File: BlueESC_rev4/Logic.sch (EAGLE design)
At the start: 37 parts, among them U1 ATMEGA168, U2 V_REG_LDOSMD, Y1 RESONATORSMD

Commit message: Commit before major changes to rev 4
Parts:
- R15: value 22 -> 150
- R16: value 22 -> 100
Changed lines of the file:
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@@
 <part name="GND9" library="SparkFun" deviceset="GND" device=""/>
 <part name="Y1" library="SparkFun" deviceset="RESONATOR" device="SMD"/>
-<part name="R15" library="SparkFun" deviceset="RESISTOR" device="0603-RES" value="22"/>
+<part name="R15" library="SparkFun" deviceset="RESISTOR" device="0603-RES" value="150"/>
 <part name="LED2" library="SparkFun" deviceset="LED" device="-3MM-NO_SILK" value="BLUE"/>
-<part name="R16" library="SparkFun" deviceset="RESISTOR" device="0603-RES" value="22"/>
+<part name="R16" library="SparkFun" deviceset="RESISTOR" device="0603-RES" value="100"/>
 <part name="LED1" library="SparkFun" deviceset="LED" device="-3MM-NO_SILK" value="RED"/>
 <part name="GND7" library="SparkFun" deviceset="GND" device=""/>

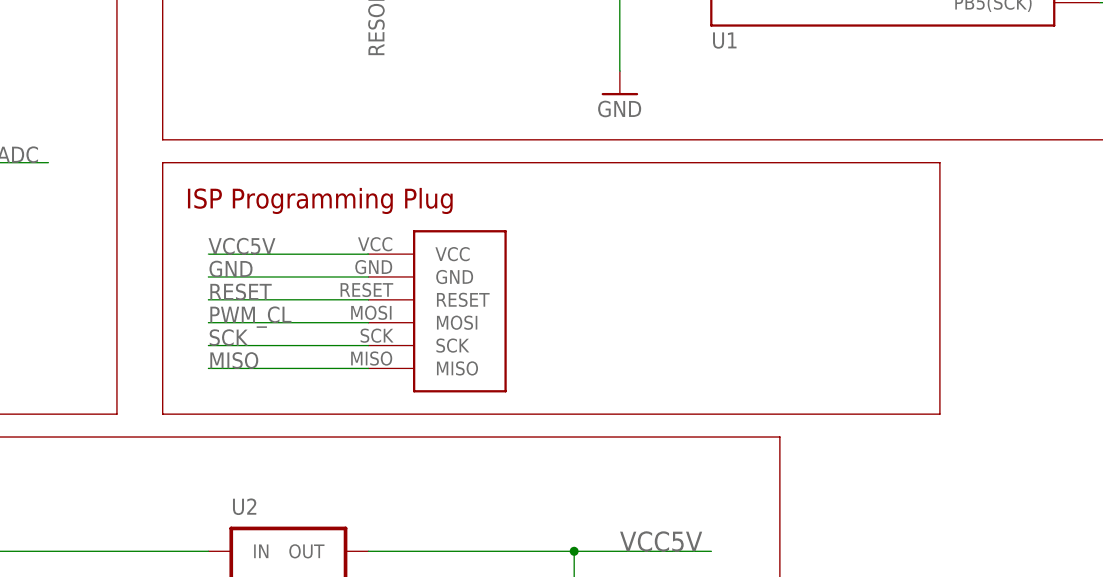
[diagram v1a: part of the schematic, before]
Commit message: Major updates on revision 4 include rearranged components, removal of programming pins, and new board shapes.
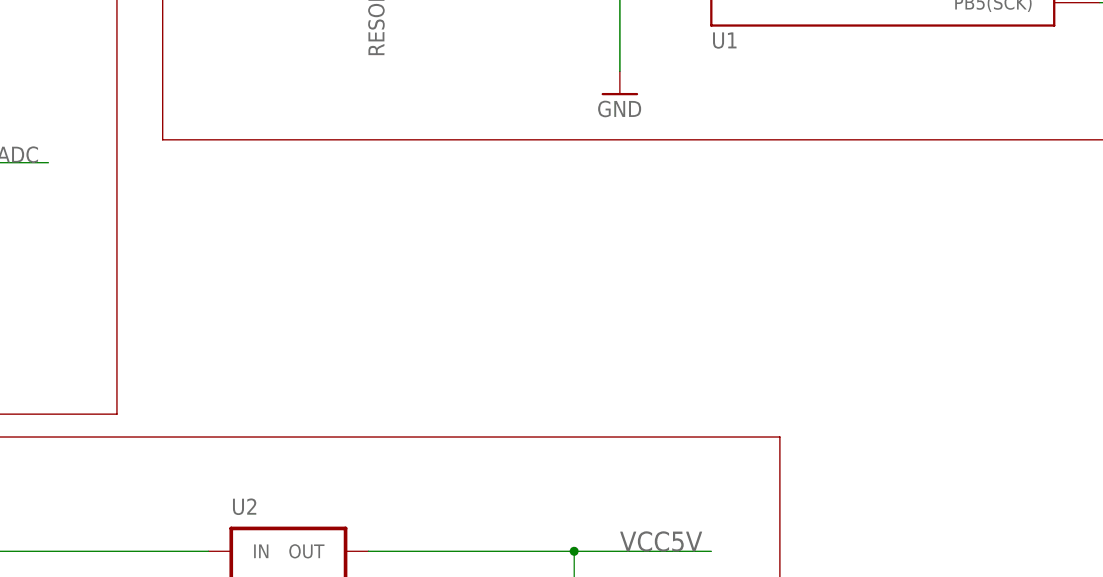
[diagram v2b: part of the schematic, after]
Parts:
- removed U$14: AVR-ISPTINY-SMD, BR-Eagle-Library:AVR-ISPTINY-SMD
- U$4: value LOGOBR-LOGO-S -> LOGOBR-LOGO-M; device BR-Eagle-Library:LOGOBR-LOGO-S -> BR-Eagle-Library:LOGOBR-LOGO-M
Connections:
- net GND: no longer U$14.GND
- net MISO: no longer U$14.MISO
- net PWM_CL: no longer U$14.MOSI
- net RESET: no longer U$14.RESET
- net SCK: no longer U$14.SCK
- net VCC5V: no longer U$14.VCC
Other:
- note removed: "ISP Programming Plug"
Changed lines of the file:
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@@
 <grid distance="0.1" unitdist="inch" unit="inch" style="lines" multiple="1" display="no" altdistance="0.01" altunitdist="inch" altunit="inch"/>
 <layers>
-<layer number="1" name="Top" color="4" fill="1" visible="no" active="no"/>
-<layer number="2" name="Route2" color="1" fill="3" visible="no" active="no"/>
-<layer number="3" name="Route3" color="4" fill="3" visible="no" active="no"/>
-<layer number="14" name="Route14" color="1" fill="6" visible="no" active="no"/>
-<layer number="15" name="Route15" color="4" fill="6" visible="no" active="no"/>
-<layer number="16" name="Bottom" color="1" fill="1" visible="no" active="no"/>
-<layer number="17" name="Pads" color="2" fill="1" visible="no" active="no"/>
-<layer number="18" name="Vias" color="2" fill="1" visible="no" active="no"/>
-<layer number="19" name="Unrouted" color="6" fill="1" visible="no" active="no"/>
-<layer number="20" name="Dimension" color="15" fill="1" visible="no" active="no"/>
-<layer number="21" name="tPlace" color="7" fill="1" visible="no" active="no"/>
-<layer number="22" name="bPlace" color="7" fill="1" visible="no" active="no"/>
-<layer number="23" name="tOrigins" color="15" fill="1" visible="no" active="no"/>
-<layer number="24" name="bOrigins" color="15" fill="1" visible="no" active="no"/>
-<layer number="25" name="tNames" color="7" fill="1" visible="no" active="no"/>
-<layer number="26" name="bNames" color="7" fill="1" visible="no" active="no"/>
-<layer number="27" name="tValues" color="7" fill="1" visible="no" active="no"/>
-<layer number="28" name="bValues" color="7" fill="1" visible="no" active="no"/>
+<layer number="1" name="Top" color="4" fill="1" visible="yes" active="no"/>
+<layer number="2" name="Route2" color="1" fill="3" visible="yes" active="no"/>
+<layer number="3" name="Route3" color="4" fill="3" visible="yes" active="no"/>
+<layer number="14" name="Route14" color="1" fill="6" visible="yes" active="no"/>
+<layer number="15" name="Route15" color="4" fill="6" visible="yes" active="no"/>
+<layer number="16" name="Bottom" color="1" fill="1" visible="yes" active="no"/>
+<layer number="17" name="Pads" color="2" fill="1" visible="yes" active="no"/>
+<layer number="18" name="Vias" color="2" fill="1" visible="yes" active="no"/>
+<layer number="19" name="Unrouted" color="6" fill="1" visible="yes" active="no"/>
+<layer number="20" name="Dimension" color="15" fill="1" visible="yes" active="no"/>
+<layer number="21" name="tPlace" color="7" fill="1" visible="yes" active="no"/>
+<layer number="22" name="bPlace" color="7" fill="1" visible="yes" active="no"/>
+<layer number="23" name="tOrigins" color="15" fill="1" visible="yes" active="no"/>
+<layer number="24" name="bOrigins" color="15" fill="1" visible="yes" active="no"/>
+<layer number="25" name="tNames" color="7" fill="1" visible="yes" active="no"/>
+<layer number="26" name="bNames" color="7" fill="1" visible="yes" active="no"/>
+<layer number="27" name="tValues" color="7" fill="1" visible="yes" active="no"/>
+<layer number="28" name="bValues" color="7" fill="1" visible="yes" active="no"/>
 <layer number="29" name="tStop" color="7" fill="3" visible="no" active="no"/>
 <layer number="30" name="bStop" color="7" fill="6" visible="no" active="no"/>
@@
 <layer number="35" name="tGlue" color="7" fill="4" visible="no" active="no"/>
 <layer number="36" name="bGlue" color="7" fill="5" visible="no" active="no"/>
-<layer number="37" name="tTest" color="7" fill="1" visible="no" active="no"/>
-<layer number="38" name="bTest" color="7" fill="1" visible="no" active="no"/>
+<layer number="37" name="tTest" color="7" fill="1" visible="yes" active="no"/>
+<layer number="38" name="bTest" color="7" fill="1" visible="yes" active="no"/>
 <layer number="39" name="tKeepout" color="4" fill="11" visible="no" active="no"/>
 <layer number="40" name="bKeepout" color="1" fill="11" visible="no" active="no"/>
@@
 <layer number="44" name="Drills" color="7" fill="1" visible="no" active="no"/>
 <layer number="45" name="Holes" color="7" fill="1" visible="no" active="no"/>
-<layer number="46" name="Milling" color="3" fill="1" visible="no" active="no"/>
-<layer number="47" name="Measures" color="7" fill="1" visible="no" active="no"/>
-<layer number="48" name="Document" color="7" fill="1" visible="no" active="no"/>
-<layer number="49" name="Reference" color="7" fill="1" visible="no" active="no"/>
-<layer number="50" name="dxf" color="7" fill="1" visible="no" active="no"/>
-<layer number="51" name="tDocu" color="7" fill="1" visible="no" active="no"/>
-<layer number="52" name="bDocu" color="7" fill="1" visible="no" active="no"/>
-<layer number="53" name="tGND_GNDA" color="7" fill="9" visible="no" active="no"/>
-<layer number="54" name="bGND_GNDA" color="1" fill="9" visible="no" active="no"/>
-<layer number="56" name="wert" color="7" fill="1" visible="no" active="no"/>
-<layer number="57" name="tCAD" color="7" fill="1" visible="no" active="no"/>
+<layer number="46" name="Milling" color="3" fill="1" visible="yes" active="no"/>
+<layer number="47" name="Measures" color="7" fill="1" visible="yes" active="no"/>
+<layer number="48" name="Document" color="7" fill="1" visible="yes" active="no"/>
+<layer number="49" name="Reference" color="7" fill="1" visible="yes" active="no"/>
+<layer number="50" name="dxf" color="7" fill="1" visible="yes" active="no"/>
+<layer number="51" name="tDocu" color="7" fill="1" visible="yes" active="no"/>
+<layer number="52" name="bDocu" color="7" fill="1" visible="yes" active="no"/>
+<layer number="53" name="tGND_GNDA" color="7" fill="9" visible="yes" active="no"/>
+<layer number="54" name="bGND_GNDA" color="1" fill="9" visible="yes" active="no"/>
+<layer number="56" name="wert" color="7" fill="1" visible="yes" active="no"/>
+<layer number="57" name="tCAD" color="7" fill="1" visible="yes" active="no"/>
 <layer number="91" name="Nets" color="2" fill="1" visible="yes" active="yes"/>
 <layer number="92" name="Busses" color="1" fill="1" visible="yes" active="yes"/>
@@
 <part name="GND21" library="SparkFun-Aesthetics" deviceset="GND" device=""/>
 <part name="GND22" library="SparkFun-Aesthetics" deviceset="GND" device=""/>
-<part name="U$4" library="BR-Eagle-Library" deviceset="LOGO" device="BR-LOGO-S" value="LOGOBR-LOGO-S"/>
+<part name="U$4" library="BR-Eagle-Library" deviceset="LOGO" device="BR-LOGO-M" value="LOGOBR-LOGO-M"/>
 <part name="U$3" library="BR-Eagle-Library" deviceset="PAD" device="1.5X3MM"/>
 <part name="U$8" library="BR-Eagle-Library" deviceset="PAD" device="1.5X3MM"/>
@@
 <part name="U$12" library="BR-Eagle-Library" deviceset="PAD" device="1.5X3MM"/>
 <part name="U$13" library="BR-Eagle-Library" deviceset="PAD" device="1.5X3MM"/>
-<part name="U$14" library="BR-Eagle-Library" deviceset="AVR-ISP" device="TINY-SMD"/>
 <part name="LOGO1" library="SparkFun-Aesthetics" deviceset="OSHW-LOGO" device="S"/>
 <part name="C4" library="SparkFun-Capacitors" deviceset="CAP" device="0603-CAP" value="0.1uF"/>
@@
 <wire x1="68.58" y1="198.12" x2="68.58" y2="261.62" width="0.1524" layer="94"/>
 <text x="71.12" y="256.54" size="2.1844" layer="94" ratio="13">Phase Sensing</text>
-<wire x1="40.64" y1="86.36" x2="127" y2="86.36" width="0.1524" layer="94"/>
-<wire x1="127" y1="86.36" x2="127" y2="58.42" width="0.1524" layer="94"/>
-<wire x1="127" y1="58.42" x2="40.64" y2="58.42" width="0.1524" layer="94"/>
-<wire x1="40.64" y1="58.42" x2="40.64" y2="86.36" width="0.1524" layer="94"/>
-<text x="43.18" y="81.28" size="2.1844" layer="94" ratio="13">ISP Programming Plug</text>
 <wire x1="-10.16" y1="124.46" x2="35.56" y2="124.46" width="0.1524" layer="94"/>
 <wire x1="35.56" y1="124.46" x2="35.56" y2="58.42" width="0.1524" layer="94"/>
@@
 <instance part="U$12" gate="G$1" x="43.18" y="-2.54"/>
 <instance part="U$13" gate="G$1" x="43.18" y="-10.16"/>
-<instance part="U$14" gate="G$1" x="68.58" y="60.96"/>
 <instance part="LOGO1" gate="G$1" x="88.9" y="-25.4"/>
 <instance part="C4" gate="G$1" x="190.5" y="63.5"/>
@@
 <wire x1="-5.08" y1="-2.54" x2="5.08" y2="-2.54" width="0.1524" layer="91"/>
 <label x="-5.08" y="-2.54" size="1.778" layer="95"/>
-</segment>
-<segment>
-<pinref part="U$14" gate="G$1" pin="GND"/>
-<wire x1="45.72" y1="73.66" x2="63.5" y2="73.66" width="0.1524" layer="91"/>
-<label x="45.72" y="73.66" size="1.778" layer="95"/>
 </segment>
 <segment>
@@
 </segment>
 <segment>
-<pinref part="U$14" gate="G$1" pin="VCC"/>
-<wire x1="63.5" y1="76.2" x2="45.72" y2="76.2" width="0.1524" layer="91"/>
-<label x="45.72" y="76.2" size="1.778" layer="95"/>
-</segment>
-<segment>
 <pinref part="C4" gate="G$1" pin="1"/>
 <wire x1="190.5" y1="68.58" x2="190.5" y2="76.2" width="0.1524" layer="91"/>
@@
 <label x="50.8" y="-88.9" size="1.778" layer="95"/>
 <pinref part="U$17" gate="G$1" pin="10"/>
-</segment>
-<segment>
-<pinref part="U$14" gate="G$1" pin="MOSI"/>
-<wire x1="45.72" y1="68.58" x2="63.5" y2="68.58" width="0.1524" layer="91"/>
-<label x="45.72" y="68.58" size="1.778" layer="95"/>
 </segment>
 <segment>
@@
 <label x="154.94" y="106.68" size="1.778" layer="95"/>
 </segment>
-<segment>
-<pinref part="U$14" gate="G$1" pin="MISO"/>
-<wire x1="45.72" y1="63.5" x2="63.5" y2="63.5" width="0.1524" layer="91"/>
-<label x="45.72" y="63.5" size="1.778" layer="95"/>
-</segment>
 </net>
 <net name="SCK" class="0">
@@
 <wire x1="144.78" y1="104.14" x2="167.64" y2="104.14" width="0.1524" layer="91"/>
 <label x="154.94" y="104.14" size="1.778" layer="95"/>
-</segment>
-<segment>
-<pinref part="U$14" gate="G$1" pin="SCK"/>
-<wire x1="63.5" y1="66.04" x2="45.72" y2="66.04" width="0.1524" layer="91"/>
-<label x="45.72" y="66.04" size="1.778" layer="95"/>
 </segment>
 </net>
@@
 <label x="58.42" y="162.56" size="1.778" layer="95" ratio="9"/>
 </segment>
-<segment>
-<pinref part="U$14" gate="G$1" pin="RESET"/>
-<wire x1="45.72" y1="71.12" x2="63.5" y2="71.12" width="0.1524" layer="91"/>
-<label x="45.72" y="71.12" size="1.778" layer="95"/>
-</segment>
-</net>
+</net>

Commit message: Minor changes before ordering production boards.
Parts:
- R15: value 150 -> 2.2K
- R16: value 100 -> 150
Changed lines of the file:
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@@
 <grid distance="0.1" unitdist="inch" unit="inch" style="lines" multiple="1" display="no" altdistance="0.01" altunitdist="inch" altunit="inch"/>
 <layers>
-<layer number="1" name="Top" color="4" fill="1" visible="yes" active="no"/>
-<layer number="2" name="Route2" color="1" fill="3" visible="yes" active="no"/>
-<layer number="3" name="Route3" color="4" fill="3" visible="yes" active="no"/>
-<layer number="14" name="Route14" color="1" fill="6" visible="yes" active="no"/>
-<layer number="15" name="Route15" color="4" fill="6" visible="yes" active="no"/>
-<layer number="16" name="Bottom" color="1" fill="1" visible="yes" active="no"/>
-<layer number="17" name="Pads" color="2" fill="1" visible="yes" active="no"/>
-<layer number="18" name="Vias" color="2" fill="1" visible="yes" active="no"/>
-<layer number="19" name="Unrouted" color="6" fill="1" visible="yes" active="no"/>
-<layer number="20" name="Dimension" color="15" fill="1" visible="yes" active="no"/>
-<layer number="21" name="tPlace" color="7" fill="1" visible="yes" active="no"/>
-<layer number="22" name="bPlace" color="7" fill="1" visible="yes" active="no"/>
-<layer number="23" name="tOrigins" color="15" fill="1" visible="yes" active="no"/>
-<layer number="24" name="bOrigins" color="15" fill="1" visible="yes" active="no"/>
-<layer number="25" name="tNames" color="7" fill="1" visible="yes" active="no"/>
-<layer number="26" name="bNames" color="7" fill="1" visible="yes" active="no"/>
-<layer number="27" name="tValues" color="7" fill="1" visible="yes" active="no"/>
-<layer number="28" name="bValues" color="7" fill="1" visible="yes" active="no"/>
+<layer number="1" name="Top" color="4" fill="1" visible="no" active="no"/>
+<layer number="2" name="Route2" color="1" fill="3" visible="no" active="no"/>
+<layer number="3" name="Route3" color="4" fill="3" visible="no" active="no"/>
+<layer number="14" name="Route14" color="1" fill="6" visible="no" active="no"/>
+<layer number="15" name="Route15" color="4" fill="6" visible="no" active="no"/>
+<layer number="16" name="Bottom" color="1" fill="1" visible="no" active="no"/>
+<layer number="17" name="Pads" color="2" fill="1" visible="no" active="no"/>
+<layer number="18" name="Vias" color="2" fill="1" visible="no" active="no"/>
+<layer number="19" name="Unrouted" color="6" fill="1" visible="no" active="no"/>
+<layer number="20" name="Dimension" color="15" fill="1" visible="no" active="no"/>
+<layer number="21" name="tPlace" color="7" fill="1" visible="no" active="no"/>
+<layer number="22" name="bPlace" color="7" fill="1" visible="no" active="no"/>
+<layer number="23" name="tOrigins" color="15" fill="1" visible="no" active="no"/>
+<layer number="24" name="bOrigins" color="15" fill="1" visible="no" active="no"/>
+<layer number="25" name="tNames" color="7" fill="1" visible="no" active="no"/>
+<layer number="26" name="bNames" color="7" fill="1" visible="no" active="no"/>
+<layer number="27" name="tValues" color="7" fill="1" visible="no" active="no"/>
+<layer number="28" name="bValues" color="7" fill="1" visible="no" active="no"/>
 <layer number="29" name="tStop" color="7" fill="3" visible="no" active="no"/>
 <layer number="30" name="bStop" color="7" fill="6" visible="no" active="no"/>
@@
 <layer number="35" name="tGlue" color="7" fill="4" visible="no" active="no"/>
 <layer number="36" name="bGlue" color="7" fill="5" visible="no" active="no"/>
-<layer number="37" name="tTest" color="7" fill="1" visible="yes" active="no"/>
-<layer number="38" name="bTest" color="7" fill="1" visible="yes" active="no"/>
+<layer number="37" name="tTest" color="7" fill="1" visible="no" active="no"/>
+<layer number="38" name="bTest" color="7" fill="1" visible="no" active="no"/>
 <layer number="39" name="tKeepout" color="4" fill="11" visible="no" active="no"/>
 <layer number="40" name="bKeepout" color="1" fill="11" visible="no" active="no"/>
@@
 <layer number="44" name="Drills" color="7" fill="1" visible="no" active="no"/>
 <layer number="45" name="Holes" color="7" fill="1" visible="no" active="no"/>
-<layer number="46" name="Milling" color="3" fill="1" visible="yes" active="no"/>
-<layer number="47" name="Measures" color="7" fill="1" visible="yes" active="no"/>
-<layer number="48" name="Document" color="7" fill="1" visible="yes" active="no"/>
-<layer number="49" name="Reference" color="7" fill="1" visible="yes" active="no"/>
-<layer number="50" name="dxf" color="7" fill="1" visible="yes" active="no"/>
-<layer number="51" name="tDocu" color="7" fill="1" visible="yes" active="no"/>
-<layer number="52" name="bDocu" color="7" fill="1" visible="yes" active="no"/>
-<layer number="53" name="tGND_GNDA" color="7" fill="9" visible="yes" active="no"/>
-<layer number="54" name="bGND_GNDA" color="1" fill="9" visible="yes" active="no"/>
-<layer number="56" name="wert" color="7" fill="1" visible="yes" active="no"/>
-<layer number="57" name="tCAD" color="7" fill="1" visible="yes" active="no"/>
+<layer number="46" name="Milling" color="3" fill="1" visible="no" active="no"/>
+<layer number="47" name="Measures" color="7" fill="1" visible="no" active="no"/>
+<layer number="48" name="Document" color="7" fill="1" visible="no" active="no"/>
+<layer number="49" name="Reference" color="7" fill="1" visible="no" active="no"/>
+<layer number="50" name="dxf" color="7" fill="1" visible="no" active="no"/>
+<layer number="51" name="tDocu" color="7" fill="1" visible="no" active="no"/>
+<layer number="52" name="bDocu" color="7" fill="1" visible="no" active="no"/>
+<layer number="53" name="tGND_GNDA" color="7" fill="9" visible="no" active="no"/>
+<layer number="54" name="bGND_GNDA" color="1" fill="9" visible="no" active="no"/>
+<layer number="56" name="wert" color="7" fill="1" visible="no" active="no"/>
+<layer number="57" name="tCAD" color="7" fill="1" visible="no" active="no"/>
 <layer number="91" name="Nets" color="2" fill="1" visible="yes" active="yes"/>
 <layer number="92" name="Busses" color="1" fill="1" visible="yes" active="yes"/>
@@
 <part name="GND9" library="SparkFun" deviceset="GND" device=""/>
 <part name="Y1" library="SparkFun" deviceset="RESONATOR" device="SMD"/>
-<part name="R15" library="SparkFun" deviceset="RESISTOR" device="0603-RES" value="150"/>
+<part name="R15" library="SparkFun" deviceset="RESISTOR" device="0603-RES" value="2.2K"/>
 <part name="LED2" library="SparkFun" deviceset="LED" device="-3MM-NO_SILK" value="BLUE"/>
-<part name="R16" library="SparkFun" deviceset="RESISTOR" device="0603-RES" value="100"/>
+<part name="R16" library="SparkFun" deviceset="RESISTOR" device="0603-RES" value="150"/>
 <part name="LED1" library="SparkFun" deviceset="LED" device="-3MM-NO_SILK" value="RED"/>
 <part name="GND7" library="SparkFun" deviceset="GND" device=""/>
